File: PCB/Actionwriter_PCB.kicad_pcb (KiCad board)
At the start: 2 copper layers, 20 parts, among them J1 Conn_01x01, U1 74HC595, U2 74HC595

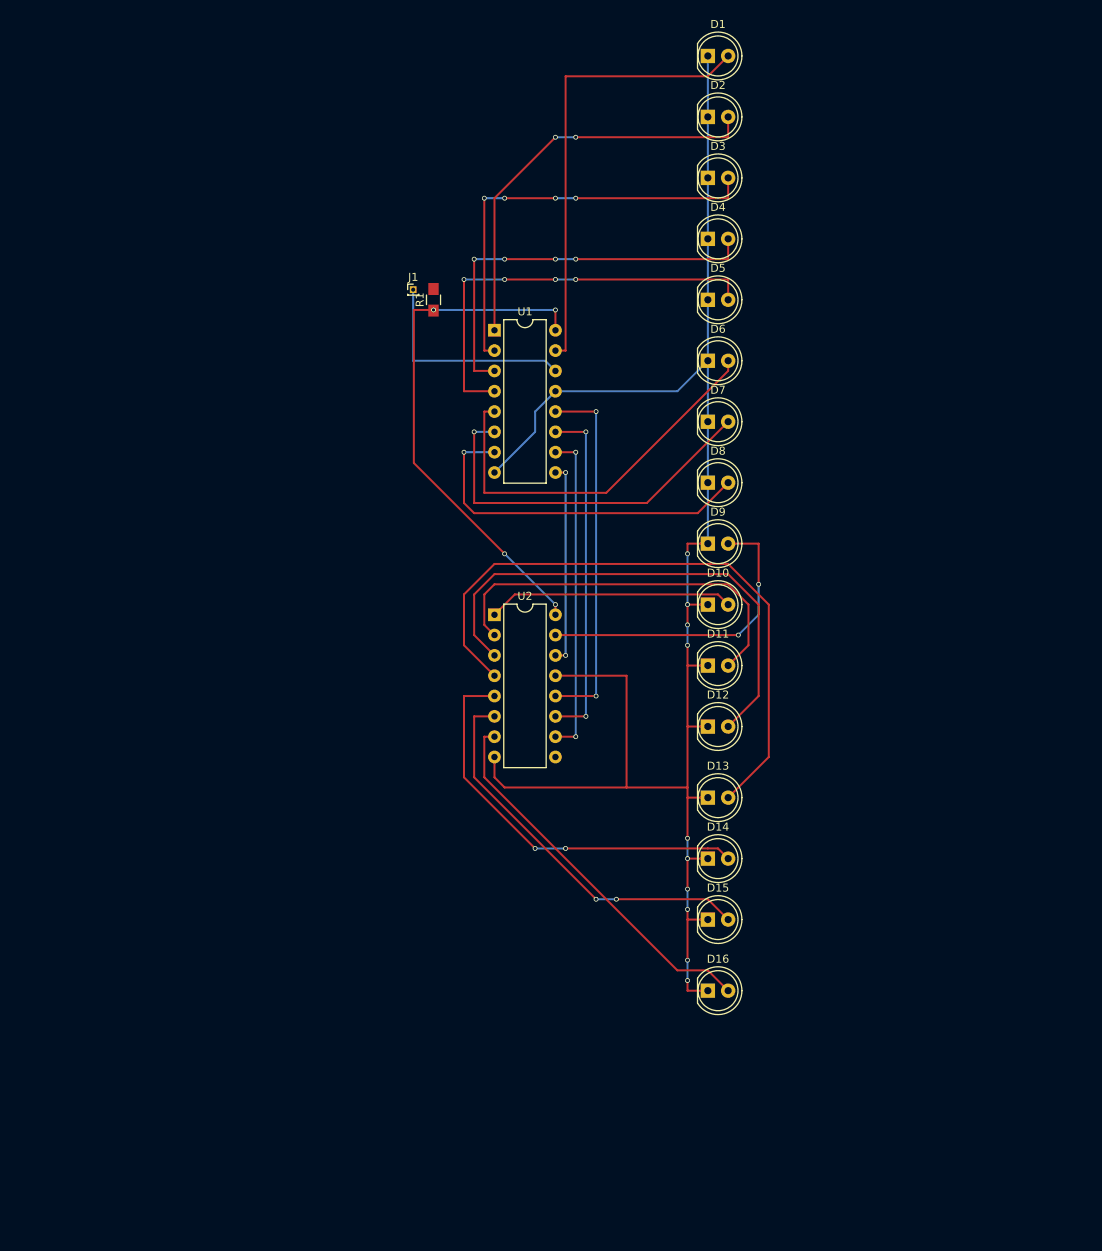
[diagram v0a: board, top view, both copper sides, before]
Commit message: Schematic seems finished
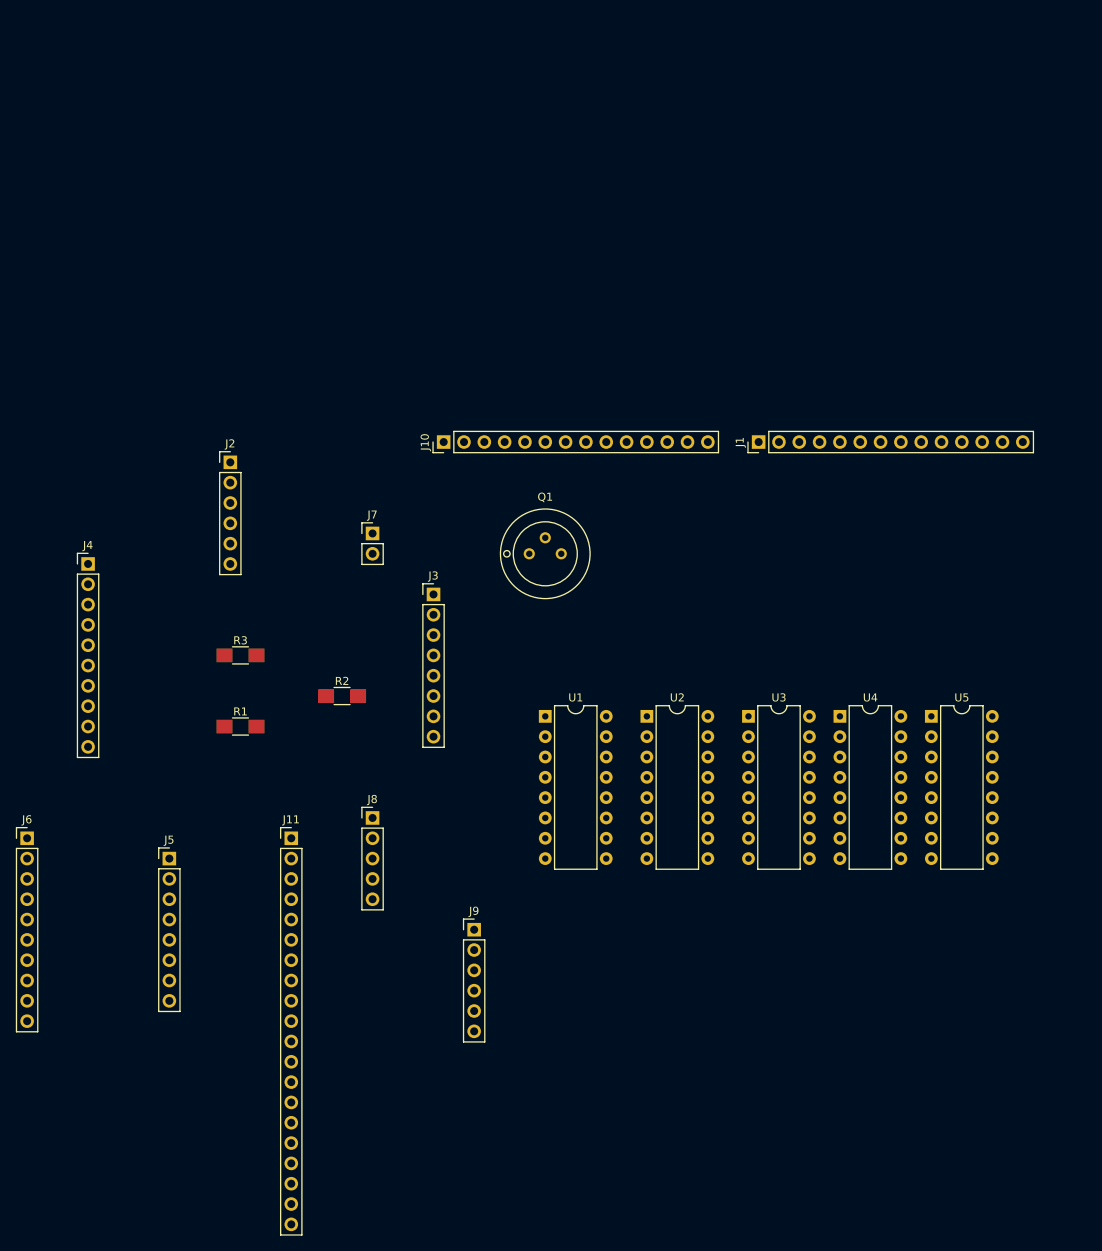
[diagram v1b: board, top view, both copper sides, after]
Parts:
- removed D1, D10, D11, D12, D13, D14, D15, D16, D2, D3, D4, D5, D6, D7, D8, D9: LED, LEDs:LED_D5.0mm
- added J10: Conn_01x14, Pin_Headers:Pin_Header_Straight_1x14_Pitch2.54mm, F.Cu at (163.8, 87.6)
- added J11: Conn_01x20, Pin_Headers:Pin_Header_Straight_1x20_Pitch2.54mm, F.Cu at (144.8, 137.2)
- added J2: Conn_01x06, Pin_Headers:Pin_Header_Straight_1x06_Pitch2.54mm, F.Cu at (137.2, 90.2)
- added J3: Conn_01x08, Pin_Headers:Pin_Header_Straight_1x08_Pitch2.54mm, F.Cu at (162.6, 106.7)
- added J4: Conn_01x10, Pin_Headers:Pin_Header_Straight_1x10_Pitch2.54mm, F.Cu at (119.4, 102.9)
- added J5: Conn_01x08, Pin_Headers:Pin_Header_Straight_1x08_Pitch2.54mm, F.Cu at (129.5, 139.7)
- added J6: Conn_01x10, Pin_Headers:Pin_Header_Straight_1x10_Pitch2.54mm, F.Cu at (111.8, 137.2)
- added J7: Conn_01x02, Pin_Headers:Pin_Header_Straight_1x02_Pitch2.54mm, F.Cu at (154.9, 99.1)
- added J8: Conn_01x05, Pin_Headers:Pin_Header_Straight_1x05_Pitch2.54mm, F.Cu at (154.9, 134.6)
- added J9: Conn_01x06, Pin_Headers:Pin_Header_Straight_1x06_Pitch2.54mm, F.Cu at (167.6, 148.6)
- added Q1: Q_NPN_EBC, Transistors_OldSowjetAera:OldSowjetaera_Transistor_Type-II_SmallPads, F.Cu at (176.5, 101.6)
- added R2: 10K, Resistors_SMD:R_1206_HandSoldering, F.Cu at (151.1, 119.4)
- added R3: 1K, Resistors_SMD:R_1206_HandSoldering, F.Cu at (138.4, 114.3)
- added U3: 4051, Housings_DIP:DIP-16_W7.62mm, F.Cu at (201.9, 121.9)
- added U4: 4051, Housings_DIP:DIP-16_W7.62mm, F.Cu at (213.4, 121.9)
- added U5: 4051, Housings_DIP:DIP-16_W7.62mm, F.Cu at (224.8, 121.9)
- J1: value Conn_01x01 -> Conn_01x14; footprint Pin_Headers:Pin_Header_Straight_1x01_Pitch1.00mm -> Pin_Headers:Pin_Header_Straight_1x14_Pitch2.54mm
- R1: value R -> 220; footprint Resistors_SMD:R_0805_HandSoldering -> Resistors_SMD:R_1206_HandSoldering
- moved R1 58.5 mm to (138.4, 123.2), turned to 0 degrees
- moved U1 48.7 mm to (176.5, 121.9)
- moved J1 47.2 mm to (203.2, 87.6), turned to 90 degrees
- moved U2 22.9 mm to (189.2, 121.9)
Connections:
- R1 pad 1: +3V3 -> Net-(J3-Pad1)
- R1 pad 2: VCC -> Net-(Q1-Pad2)
- U1 pad 10: Net-(U1-Pad10) -> GND
- U1 pad 11: Net-(U1-Pad11) -> GND
- U1 pad 14: Net-(J1-Pad1) -> Net-(J6-Pad6)
- U2 pad 10: Net-(U1-Pad10) -> GND
- U2 pad 11: Net-(U1-Pad11) -> GND
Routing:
- net GND: track 221.2 -> 0.00 mm, vias 12 -> 0
- net Net-(J11-Pad13): track 79.8 -> 0.00 mm
- net Net-(J11-Pad12): track 63.7 -> 0.00 mm
- net +3V3: track 61.9 -> 0.00 mm, vias 4 -> 0
- net Net-(J11-Pad1): track 56.9 -> 0.00 mm
- net Net-(J11-Pad3): track 53.3 -> 0.00 mm, vias 4 -> 0
- net Net-(J11-Pad5): track 53.3 -> 0.00 mm, vias 4 -> 0
- net Net-(J11-Pad2): track 51.4 -> 0.00 mm, vias 2 -> 0
- net Net-(J11-Pad14): track 51.2 -> 0.00 mm, vias 2 -> 0
- net Net-(J11-Pad4): track 50.8 -> 0.00 mm, vias 4 -> 0
- net Net-(J11-Pad6): track 49.5 -> 0.00 mm
- net Net-(J11-Pad15): track 49.3 -> 0.00 mm, vias 2 -> 0
- net Net-(J11-Pad11): track 48.9 -> 0.00 mm
- net Net-(J11-Pad16): track 47.9 -> 0.00 mm
- net Net-(J11-Pad7): track 47.4 -> 0.00 mm, vias 1 -> 0
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
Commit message: Test moving some address lines to 0 and 1 (for later use of PWM), PCB work
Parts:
- removed J1, J10: Conn_01x14, Pin_Headers:Pin_Header_Straight_1x14_Pitch2.54mm
- removed J11: Conn_01x20, Pin_Headers:Pin_Header_Straight_1x20_Pitch2.54mm
- removed J2, J9: Conn_01x06, Pin_Headers:Pin_Header_Straight_1x06_Pitch2.54mm
- removed J3, J5: Conn_01x08, Pin_Headers:Pin_Header_Straight_1x08_Pitch2.54mm
- removed J4, J6: Conn_01x10, Pin_Headers:Pin_Header_Straight_1x10_Pitch2.54mm
- removed J7: Conn_01x02, Pin_Headers:Pin_Header_Straight_1x02_Pitch2.54mm
- removed J8: Conn_01x05, Pin_Headers:Pin_Header_Straight_1x05_Pitch2.54mm
- removed Q1: Q_NPN_EBC, Transistors_OldSowjetAera:OldSowjetaera_Transistor_Type-II_SmallPads
- removed R1: 220, Resistors_SMD:R_1206_HandSoldering
- removed R2: 10K, Resistors_SMD:R_1206_HandSoldering
- removed R3: 1K, Resistors_SMD:R_1206_HandSoldering
- removed U1, U2: 74HC595, Housings_DIP:DIP-16_W7.62mm
- removed U3, U4, U5: 4051, Housings_DIP:DIP-16_W7.62mm

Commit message: updated?
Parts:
- added J1: KBD_LHS, Pin_Headers:Pin_Header_Straight_1x14_Pitch2.54mm, F.Cu at (141.0, 132.1)
- added J10: KBD_RHS, Pin_Headers:Pin_Header_Straight_1x16_Pitch2.54mm, F.Cu at (185.4, 132.1)
- added J11: LEDS0, Pin_Headers:Pin_Header_Straight_1x09_Pitch2.54mm, F.Cu at (226.1, 74.9)
- added J12: LEDS1, Pin_Headers:Pin_Header_Straight_1x09_Pitch2.54mm, F.Cu at (226.1, 101.6)
- added J13: LEDX, Pin_Headers:Pin_Header_Straight_1x04_Pitch1.27mm_SMD_Pin1Right, F.Cu at (231.1, 128.3)
- added J2: Arduino_AnalogIn, Pin_Headers:Pin_Header_Straight_1x06_Pitch2.54mm, F.Cu at (139.7, 53.3)
- added J3: Arduino_DigitalLow, Pin_Headers:Pin_Header_Straight_1x08_Pitch2.54mm, F.Cu at (139.7, 82.5)
- added J4: AIN_D8_Expander, Pin_Headers:Pin_Header_Straight_1x11_Pitch2.54mm, F.Cu at (133.3, 57.1)
- added J5: Arduino_power, Pin_Headers:Pin_Header_Straight_1x08_Pitch2.54mm, F.Cu at (168.9, 53.3)
- added J6: Arduino_DigitalHigh, Pin_Headers:Pin_Header_Straight_1x10_Pitch2.54mm, F.Cu at (165.1, 82.5)
- added J7: Reset_Jumper, Pin_Headers:Pin_Header_Straight_1x03_Pitch2.54mm, F.Cu at (158.8, 47.0)
- added J8: I2C_Expander, Pin_Headers:Pin_Header_Straight_1x05_Pitch2.54mm, F.Cu at (209.6, 78.7)
- added J9: RGB_Expander, Pin_Headers:Pin_Header_Straight_1x06_Pitch2.54mm, F.Cu at (123.2, 94.0)
- added Q1: PN2222A, TO_SOT_Packages_THT:TO-92_Molded_Narrow, F.Cu at (186.7, 90.2)
- added Q2: IRLB8721PBF, TO_SOT_Packages_THT:TO-220-3_Vertical, F.Cu at (132.1, 105.4)
- added Q3: IRLB8721PBF, TO_SOT_Packages_THT:TO-220-3_Vertical, F.Cu at (132.1, 99.1)
- added Q4: IRLB8721PBF, TO_SOT_Packages_THT:TO-220-3_Vertical, F.Cu at (132.1, 92.7)
- added R1: 220, Resistors_SMD:R_1206_HandSoldering, F.Cu at (195.6, 94.0)
- added R2: 10K, Resistors_SMD:R_1206_HandSoldering, F.Cu at (180.3, 95.2)
- added R3: 1K, Resistors_SMD:R_1206_HandSoldering, F.Cu at (160.0, 92.7)
- added U1: 74HC595, Housings_DIP:DIP-16_W7.62mm, F.Cu at (234.9, 80.0)
- added U2: 74HC595, Housings_DIP:DIP-16_W7.62mm, F.Cu at (234.9, 104.1)
- added U3: 4051, Housings_DIP:DIP-16_W7.62mm, F.Cu at (160.0, 105.4)
- added U4: 4051, Housings_DIP:DIP-16_W7.62mm, F.Cu at (142.2, 105.4)
- added U5: 4051, Housings_DIP:DIP-16_W7.62mm, F.Cu at (177.8, 102.9)
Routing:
- net GND: track 0.00 -> 321.4 mm, vias 0 -> 3
- net Net-(J3-Pad3): track 0.00 -> 116.0 mm, vias 0 -> 3
- net +3V3: track 0.00 -> 107.6 mm
- net Net-(J1-Pad1): track 0.00 -> 89.4 mm, vias 0 -> 2
- net Net-(J10-Pad8): track 0.00 -> 78.4 mm, vias 0 -> 2
- net Net-(J1-Pad14): track 0.00 -> 76.5 mm, vias 0 -> 4
- net Net-(J1-Pad2): track 0.00 -> 72.0 mm, vias 0 -> 2
- net Net-(J10-Pad6): track 0.00 -> 67.2 mm
- net Net-(J10-Pad7): track 0.00 -> 67.2 mm, vias 0 -> 1
- net Net-(J1-Pad13): track 0.00 -> 66.0 mm, vias 0 -> 1
- net Net-(J1-Pad3): track 0.00 -> 62.6 mm
- net Net-(J1-Pad4): track 0.00 -> 55.1 mm, vias 0 -> 1
- net Net-(J13-Pad3): track 0.00 -> 50.4 mm, vias 0 -> 1
- net +5V: track 0.00 -> 48.6 mm
- net Net-(J10-Pad5): track 0.00 -> 48.4 mm
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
